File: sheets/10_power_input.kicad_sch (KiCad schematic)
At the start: 36 parts, among them J1 MSTB 2,5/5-GF-5,08, J2 MSTB 2,5/2-GF-5,08, Q101 STD18NF25, Q102 IPD30N10S3L-34, U101 LM74930QRGERQ1

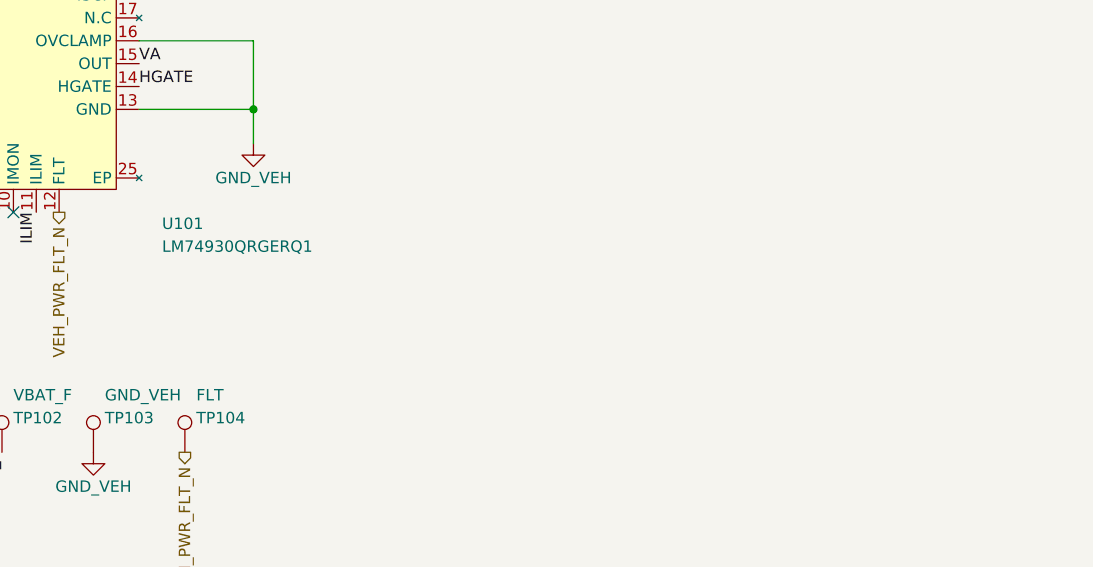
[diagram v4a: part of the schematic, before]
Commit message: Nota EP/RTN de U101, regla de PCB y verificación del FDD7N25LZ
- 10_power_input: nota visible junto a U101 "EP/RTN flotante: NO conectar
  a GND (datasheet SNOSDF6, tabla 5-1 y sección 8.3)".
- CLAUDE.md (PCB): la red del pad 25 de U101 nunca se une a GND ni a otra
  red; regla DRC personalizada al empezar el PCB.
- 70_output: Notes de Q701 con datos del datasheet: no es AEC-Q101,
  RDS(on) a 5 V (0.57 ohm máx a 25 C, ~0.91 ohm a 85 C), margen de BVDSS
  y SOA con corto a +32 V. El filtro del latch no necesita cambios.
- docs/datasheets/FDD7N25LZ.pdf.

Co-Authored-By: Claude Opus 5.5 <noreply@anthropic.com>
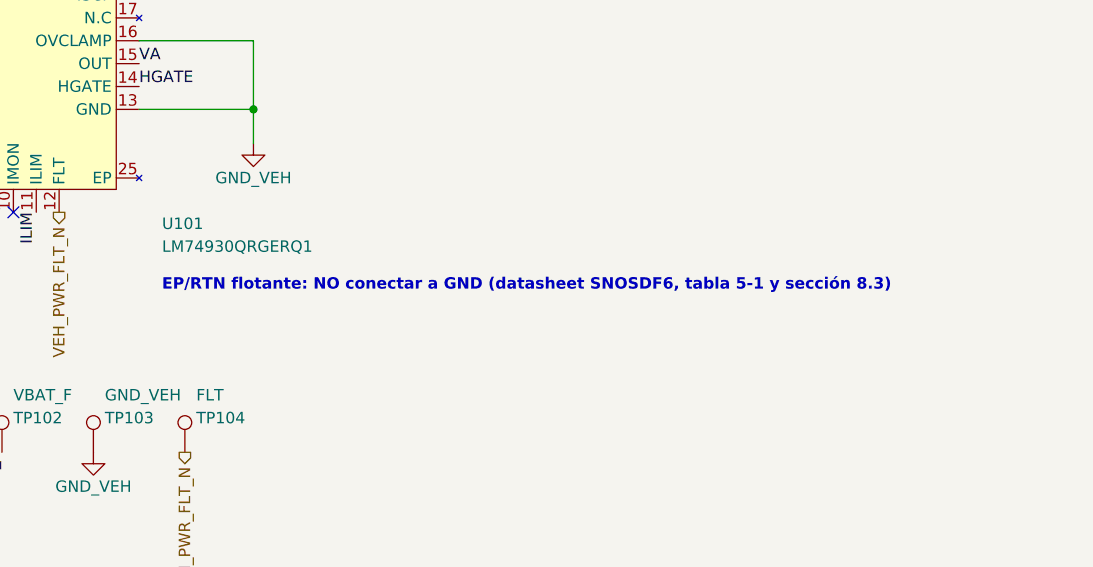
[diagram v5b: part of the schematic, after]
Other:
- note added: "EP/RTN flotante: NO conectar a GND (datasheet SNOSDF6, tabla 5-1 y sección 8.3)"
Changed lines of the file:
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@@
+		)
+	)
+	(text "EP/RTN flotante: NO conectar a GND (datasheet SNOSDF6, tabla 5-1 y sección 8.3)"
+		(exclude_from_sim no)
+		(at 152.4 133.35 0)
+		(effects
+			(font
+				(size 1.27 1.27)
+				(bold yes)
+				(color 200 0 0 1)
+			)
+			(justify left bottom)
 		)
 	)
